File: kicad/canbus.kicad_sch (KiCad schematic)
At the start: 6 parts

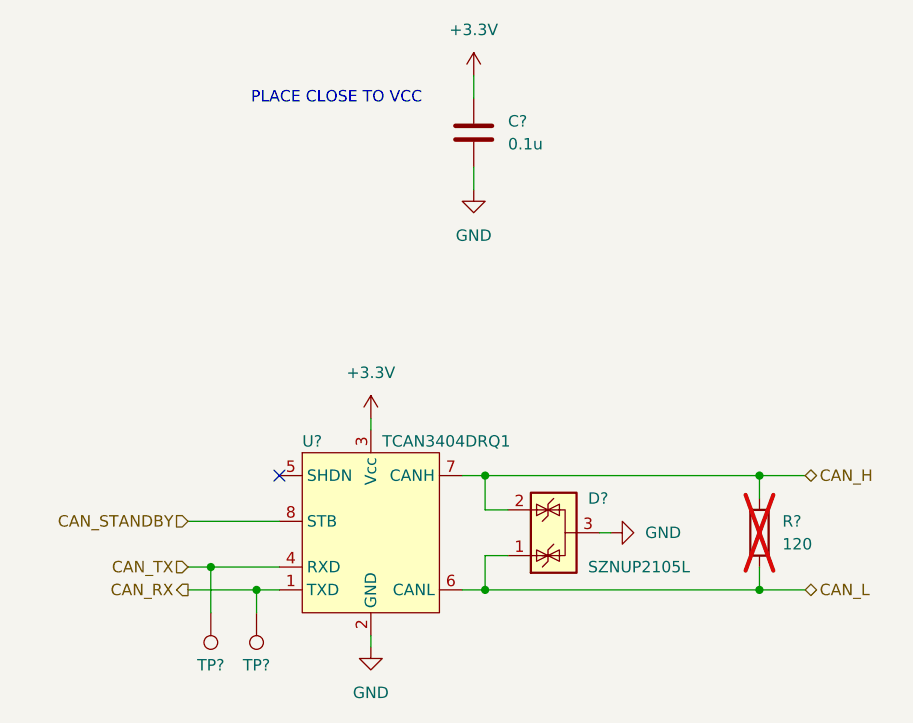
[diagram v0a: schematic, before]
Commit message: Update canbus TVS protection
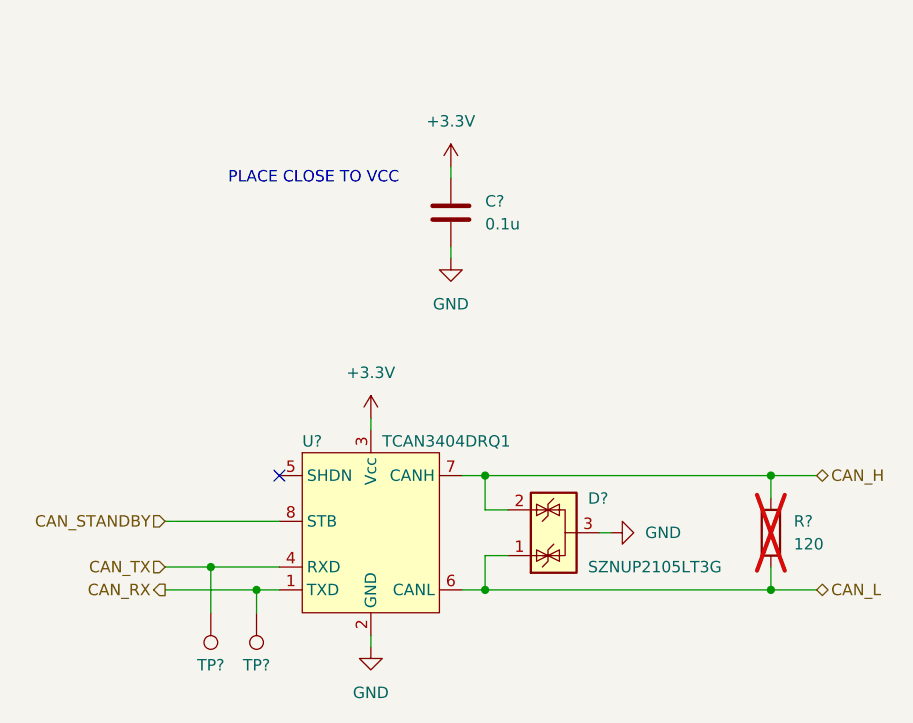
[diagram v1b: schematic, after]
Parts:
- D?: value SZNUP2105L -> SZNUP2105LT3G; Manufacturer (none) -> onsemi; Part Number (none) -> SZNUP2105LT3G
- U?: Manufacturer (none) -> Texas Instruments; Part Number (none) -> TCAN3404DRQ1
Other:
- moved on the sheet: C?, R?

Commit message: Update connector; annotate and assign footprints
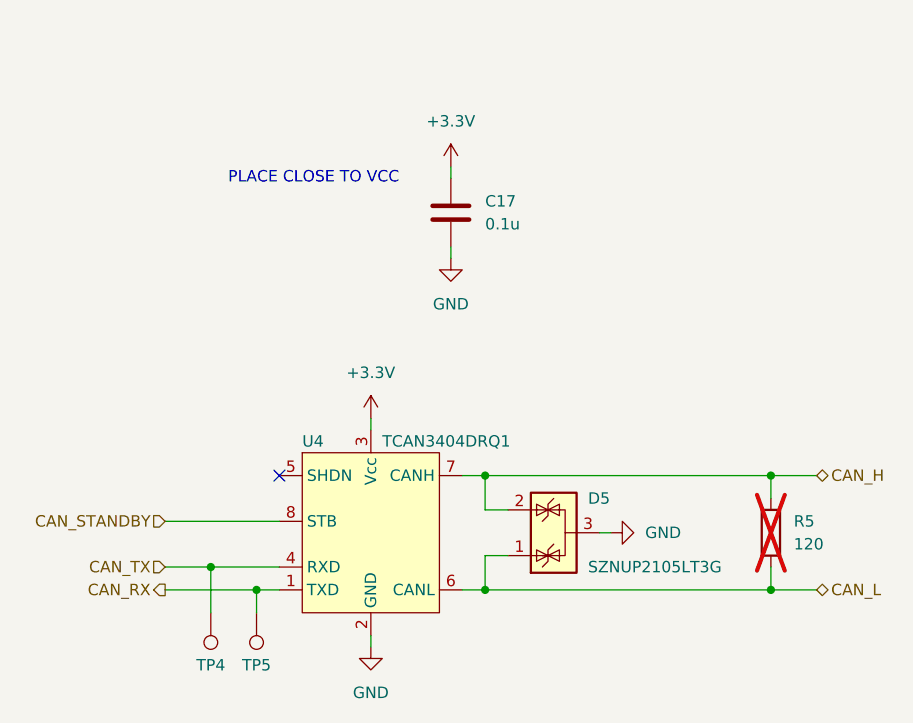
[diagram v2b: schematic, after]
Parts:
- C17: renamed from C?; footprint (none) -> Capacitor_SMD:C_0603_1608Metric
- R5: renamed from R?; footprint (none) -> Resistor_SMD:R_0603_1608Metric
- TP4, TP5: renamed from TP?; footprint (none) -> TestPoint:TestPoint_Pad_D2.0mm
- gave numbers to parts that had none: 2
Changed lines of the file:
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@@
 		(dnp no)
 		(fields_autoplaced yes)
-		(property "Reference" "#PWR?"
+		(property "Reference" "#PWR029"
 			(at 200.66 138.43 0)
 			(hide yes)
@@
 			(project "bmw-e36-abs-adapter"
 				(path "/325be93f-b4a6-4f2b-83c3-2ccd33e5cc03/1e118eea-b0b6-4052-9f03-bc9e02cc6f9e"
-					(reference "#PWR?")
+					(reference "#PWR029")
 					(unit 1)
 				)
@@
 		(in_pos_files yes)
 		(dnp no)
-		(property "Reference" "D?"
+		(property "Reference" "D5"
 			(at 224.79 143.51 90)
 			(show_name no)
@@
 			(project "bmw-e36-abs-adapter"
 				(path "/325be93f-b4a6-4f2b-83c3-2ccd33e5cc03/1e118eea-b0b6-4052-9f03-bc9e02cc6f9e"
-					(reference "D?")
+					(reference "D5")
 					(unit 1)
 				)
@@
 		(dnp no)
 		(fields_autoplaced yes)
-		(property "Reference" "#PWR?"
+		(property "Reference" "#PWR032"
 			(at 209.55 123.19 0)
 			(hide yes)
@@
 			(project "bmw-e36-abs-adapter"
 				(path "/325be93f-b4a6-4f2b-83c3-2ccd33e5cc03/1e118eea-b0b6-4052-9f03-bc9e02cc6f9e"
-					(reference "#PWR?")
+					(reference "#PWR032")
 					(unit 1)
 				)
@@
 		(dnp no)
 		(fields_autoplaced yes)
-		(property "Reference" "#PWR?"
+		(property "Reference" "#PWR030"
 			(at 200.66 166.37 0)
 			(hide yes)
@@
 			(project "bmw-e36-abs-adapter"
 				(path "/325be93f-b4a6-4f2b-83c3-2ccd33e5cc03/1e118eea-b0b6-4052-9f03-bc9e02cc6f9e"
-					(reference "#PWR?")
+					(reference "#PWR030")
 					(unit 1)
 				)
@@
 		(in_pos_files yes)
 		(dnp no)
-		(property "Reference" "TP?"
+		(property "Reference" "TP4"
 			(at 182.88 161.29 0)
 			(show_name no)
@@
 			)
 		)
-		(property "Footprint" ""
+		(property "Footprint" "TestPoint:TestPoint_Pad_D2.0mm"
 			(at 177.8 156.21 0)
 			(hide yes)
@@
 			(project "bmw-e36-abs-adapter"
 				(path "/325be93f-b4a6-4f2b-83c3-2ccd33e5cc03/1e118eea-b0b6-4052-9f03-bc9e02cc6f9e"
-					(reference "TP?")
+					(reference "TP4")
 					(unit 1)
 				)
@@
 		(dnp no)
 		(fields_autoplaced yes)
-		(property "Reference" "#PWR?"
+		(property "Reference" "#PWR033"
 			(at 233.68 147.32 0)
 			(hide yes)
@@
 			(project "bmw-e36-abs-adapter"
 				(path "/325be93f-b4a6-4f2b-83c3-2ccd33e5cc03/1e118eea-b0b6-4052-9f03-bc9e02cc6f9e"
-					(reference "#PWR?")
+					(reference "#PWR033")
 					(unit 1)
 				)
@@
 		(in_pos_files yes)
 		(dnp no)
-		(property "Reference" "TP?"
+		(property "Reference" "TP5"
 			(at 187.96 161.29 0)
 			(show_name no)
@@
 			)
 		)
-		(property "Footprint" ""
+		(property "Footprint" "TestPoint:TestPoint_Pad_D2.0mm"
 			(at 182.88 156.21 0)
 			(hide yes)
@@
 			(project "bmw-e36-abs-adapter"
 				(path "/325be93f-b4a6-4f2b-83c3-2ccd33e5cc03/1e118eea-b0b6-4052-9f03-bc9e02cc6f9e"
-					(reference "TP?")
+					(reference "TP5")
 					(unit 1)
 				)
@@
 		(dnp yes)
 		(fields_autoplaced yes)
-		(property "Reference" "R?"
+		(property "Reference" "R5"
 			(at 247.65 146.0499 0)
 			(show_name no)
@@
 			)
 		)
-		(property "Footprint" ""
+		(property "Footprint" "Resistor_SMD:R_0603_1608Metric"
 			(at 243.332 147.32 90)
 			(hide yes)
@@
 			(project "bmw-e36-abs-adapter"
 				(path "/325be93f-b4a6-4f2b-83c3-2ccd33e5cc03/1e118eea-b0b6-4052-9f03-bc9e02cc6f9e"
-					(reference "R?")
+					(reference "R5")
 					(unit 1)
 				)
@@
 		(dnp no)
 		(fields_autoplaced yes)
-		(property "Reference" "#PWR?"
+		(property "Reference" "#PWR031"
 			(at 209.55 110.49 0)
 			(hide yes)
@@
 			(project "bmw-e36-abs-adapter"
 				(path "/325be93f-b4a6-4f2b-83c3-2ccd33e5cc03/1e118eea-b0b6-4052-9f03-bc9e02cc6f9e"
-					(reference "#PWR?")
+					(reference "#PWR031")
 					(unit 1)
 				)
@@
 		(in_pos_files yes)
 		(dnp no)
-		(property "Reference" "U?"
+		(property "Reference" "U4"
 			(at 193.04 137.16 0)
 			(show_name no)
@@
 			(project "bmw-e36-abs-adapter"
 				(path "/325be93f-b4a6-4f2b-83c3-2ccd33e5cc03/1e118eea-b0b6-4052-9f03-bc9e02cc6f9e"
-					(reference "U?")
+					(reference "U4")
 					(unit 1)
 				)
@@
 		(dnp no)
 		(fields_autoplaced yes)
-		(property "Reference" "C?"
+		(property "Reference" "C17"
 			(at 213.36 110.4899 0)
 			(show_name no)
@@
 			)
 		)
-		(property "Footprint" ""
+		(property "Footprint" "Capacitor_SMD:C_0603_1608Metric"
 			(at 210.5152 115.57 0)
 			(hide yes)
@@
 			(project "bmw-e36-abs-adapter"
 				(path "/325be93f-b4a6-4f2b-83c3-2ccd33e5cc03/1e118eea-b0b6-4052-9f03-bc9e02cc6f9e"
-					(reference "C?")
-					(unit 1)
-				)
+					(reference "C17")
+					(unit 1)
+				)

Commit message: Add jumper for canbus termination
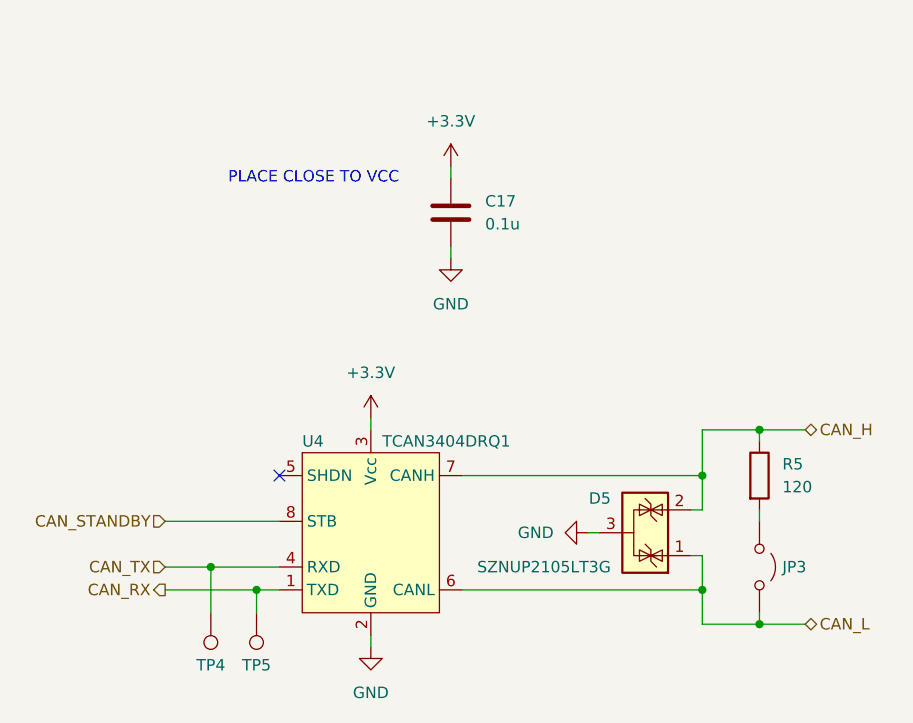
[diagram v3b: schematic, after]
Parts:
- added JP3: Jumper_2_Open, symbol symbols:Jumper_2_Open
- R5: now fitted
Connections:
- net CAN_L: now also JP3.2 (B); no longer R5.2
- new net: JP3.1 (A), R5.2
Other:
- moved on the sheet: D5

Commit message: Update footprints
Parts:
- JP3: value Jumper_2_Open -> TERM; footprint (none) -> Connector_PinHeader_2.54mm:PinHeader_1x02_P2.54mm_Vertical
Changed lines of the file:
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@@
 			)
 		)
-		(property "Value" "Jumper_2_Open"
+		(property "Value" "TERM"
 			(at 246.38 152.3999 90)
 			(hide yes)
@@
 			)
 		)
-		(property "Footprint" ""
+		(property "Footprint" "Connector_PinHeader_2.54mm:PinHeader_1x02_P2.54mm_Vertical"
 			(at 243.84 151.13 0)
 			(hide yes)

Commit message: Update part numbers and fix ERC issues
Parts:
- C17: Manufacturer (none) -> Murata; Part Number (none) -> GCJ188R71H104KA12D
- JP3: Manufacturer (none) -> Wurth; Part Number (none) -> 61300211121
- R5: Manufacturer (none) -> Panasonic; Part Number (none) -> ERJ-3EKF1200V
- TP4, TP5: now left out of the parts list
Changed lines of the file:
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@@
+			)
+		)
+		(property "Manufacturer" "Wurth"
+			(at 243.84 151.13 90)
+			(hide yes)
+			(show_name no)
+			(do_not_autoplace no)
+			(effects
+				(font
+					(size 1.27 1.27)
+				)
+			)
+		)
+		(property "Part Number" "61300211121"
+			(at 243.84 151.13 90)
+			(hide yes)
+			(show_name no)
+			(do_not_autoplace no)
+			(effects
+				(font
+					(size 1.27 1.27)
+				)
 			)
 		)
@@
 		(body_style 1)
 		(exclude_from_sim no)
-		(in_bom yes)
+		(in_bom no)
 		(on_board yes)
 		(in_pos_files yes)
@@
 		(body_style 1)
 		(exclude_from_sim no)
-		(in_bom yes)
+		(in_bom no)
 		(on_board yes)
 		(in_pos_files yes)
@@
 			)
 		)
+		(property "Manufacturer" "Panasonic"
+			(at 243.84 140.97 0)
+			(hide yes)
+			(show_name no)
+			(do_not_autoplace no)
+			(effects
+				(font
+					(size 1.27 1.27)
+				)
+			)
+		)
+		(property "Part Number" "ERJ-3EKF1200V"
+			(at 243.84 140.97 0)
+			(hide yes)
+			(show_name no)
+			(do_not_autoplace no)
+			(effects
+				(font
+					(size 1.27 1.27)
+				)
+			)
+		)
 		(pin "2"
 		)
@@
 			(at 209.55 111.76 0)
 			(hide yes)
+			(show_name no)
+			(do_not_autoplace no)
+			(effects
+				(font
+					(size 1.27 1.27)
+				)
+			)
+		)
+		(property "Manufacturer" "Murata"
+			(at 209.55 111.76 0)
+			(hide yes)
+			(show_name no)
+			(do_not_autoplace no)
+			(effects
+				(font
+					(size 1.27 1.27)
+				)
+			)
+		)
+		(property "Part Number" "GCJ188R71H104KA12D"
+			(at 209.55 111.76 0)
+			(hide yes)

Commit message: Initial placement on PCB
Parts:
- TP4, TP5: footprint TestPoint:TestPoint_Pad_D2.0mm -> TestPoint:TestPoint_Pad_D1.5mm
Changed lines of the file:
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@@
 			)
 		)
-		(property "Footprint" "TestPoint:TestPoint_Pad_D2.0mm"
+		(property "Footprint" "TestPoint:TestPoint_Pad_D1.5mm"
 			(at 177.8 156.21 0)
 			(hide yes)
@@
 			)
 		)
-		(property "Footprint" "TestPoint:TestPoint_Pad_D2.0mm"
+		(property "Footprint" "TestPoint:TestPoint_Pad_D1.5mm"
 			(at 182.88 156.21 0)
 			(hide yes)
